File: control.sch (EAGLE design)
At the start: 123 parts, among them IC3 ATTINY85-20S, U1 L293DD013TR

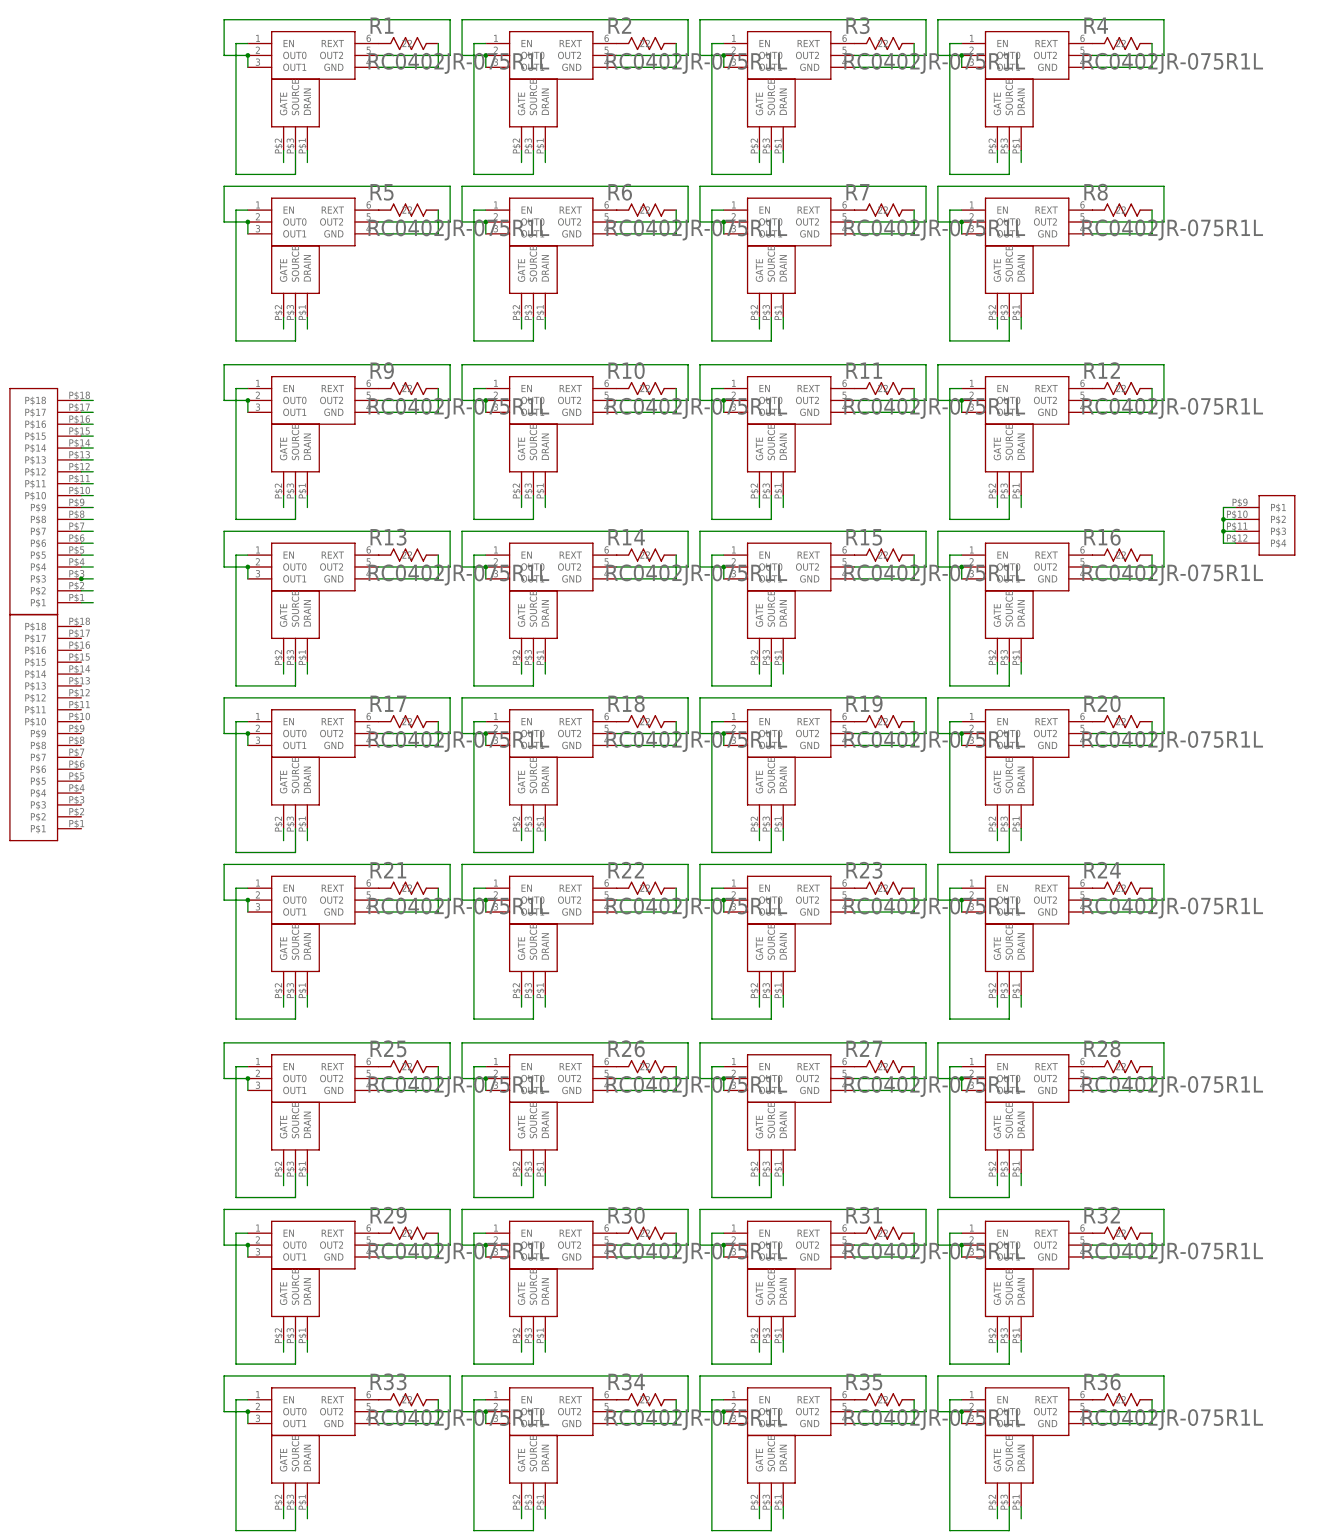
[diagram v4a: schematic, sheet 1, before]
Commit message: removes excess led controllers
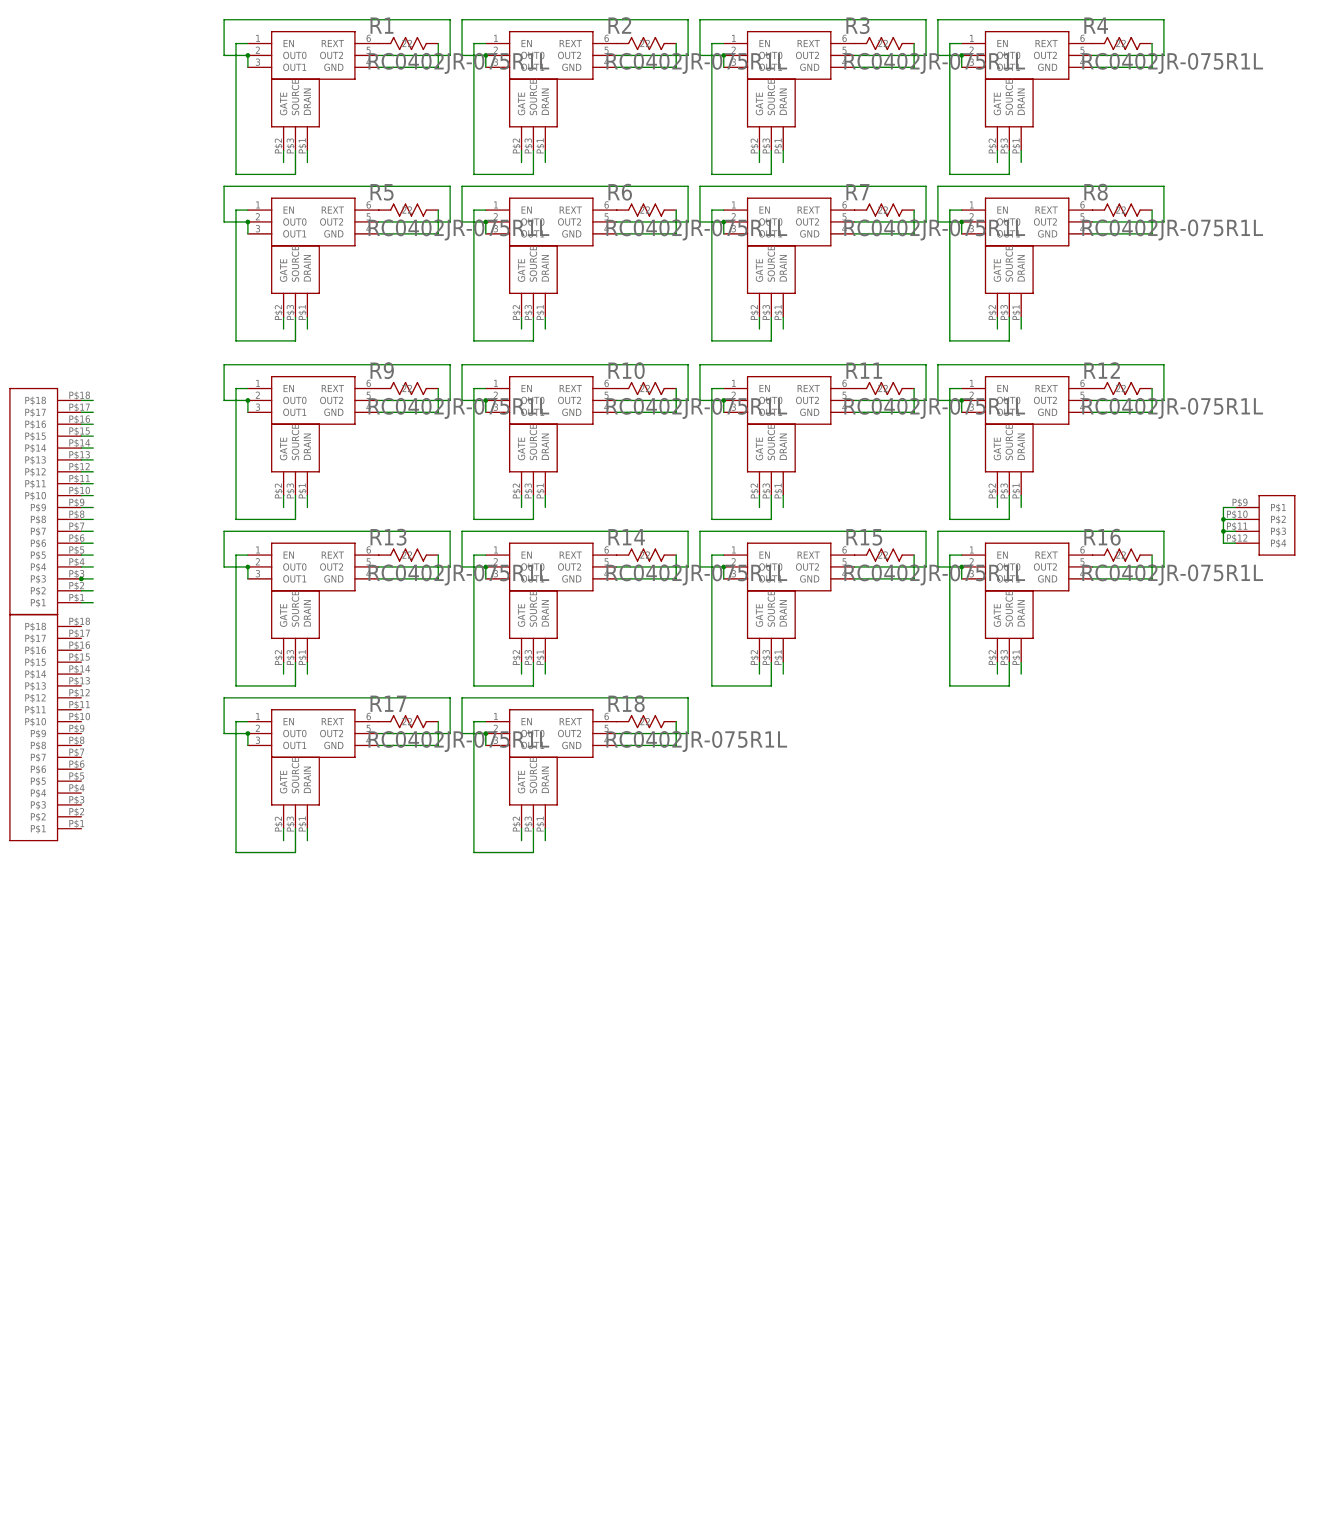
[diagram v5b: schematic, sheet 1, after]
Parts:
- removed C1: UVR0J102MPD1TA, Smile_Shade:UVR0J102MPD1TA
- removed C2: UWX1C101MCL1GB, Smile_Shade:UWX1C101MCL1GB
- removed R19, R20, R21, R22, R23, R24, R25, R26, R27, R28, R29, R30, R31, R32, R33, R34, R35, R36: RC0402JR-075R1L, Smile_Shade:RC0402JR-075R1L
- removed U$36: SRN8040-101M, Smile_Shade:SRN8040-101M
- removed U$41, U$46, U$48, U$50, U$52, U$54, U$56, U$58, U$60, U$62, U$64, U$66, U$68, U$70, U$72, U$74, U$76, U$78: 2N7002P, Smile_Shade:2N7002P
- removed U$43: LM2576HVSX-5.0/NOPB, Smile_Shade:LM2576HVSX-5.0/NOPB
- removed U$45, U$47, U$49, U$51, U$53, U$55, U$57, U$59, U$61, U$63, U$65, U$67, U$69, U$71, U$73, U$75, U$77, U$79: BCR420UW6-7, Smile_Shade:BCR420UW6-7
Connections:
- removed net 48V: C2.11
- removed net GND18: R19.11, U$41.DRAIN, U$45.GND
- removed net GND19: R20.11, U$46.DRAIN, U$47.GND
- removed net GND20: R21.11, U$48.DRAIN, U$49.GND
- removed net GND21: R22.11, U$50.DRAIN, U$51.GND
- removed net GND22: R23.11, U$52.DRAIN, U$53.GND
- removed net GND23: R24.11, U$54.DRAIN, U$55.GND
- removed net GND24: R25.11, U$56.DRAIN, U$57.GND
- removed net GND25: R26.11, U$58.DRAIN, U$59.GND
- removed net GND26: R27.11, U$60.DRAIN, U$61.GND
- removed net GND27: R28.11, U$62.DRAIN, U$63.GND
- removed net GND28: R29.11, U$64.DRAIN, U$65.GND
- removed net GND29: R30.11, U$66.DRAIN, U$67.GND
- removed net GND30: R31.11, U$68.DRAIN, U$69.GND
- removed net GND31: R32.11, U$70.DRAIN, U$71.GND
- removed net GND32: R33.11, U$72.DRAIN, U$73.GND
- removed net GND33: R34.11, U$74.DRAIN, U$75.GND
- removed net GND34: R35.11, U$76.DRAIN, U$77.GND
- removed net GND35: R36.11, U$78.DRAIN, U$79.GND
- removed net LEDSTR_33: U$45.OUT0, U$45.OUT1, U$45.OUT2
- removed net LEDSTR_34: U$47.OUT0, U$47.OUT1, U$47.OUT2
- removed net LEDSTR_35: U$49.OUT0, U$49.OUT1, U$49.OUT2
- removed net LEDSTR_36: U$51.OUT0, U$51.OUT1, U$51.OUT2
- removed net LEDSTR_37: U$53.OUT0, U$53.OUT1, U$53.OUT2
- removed net LEDSTR_38: U$55.OUT0, U$55.OUT1, U$55.OUT2
- removed net LEDSTR_39: U$57.OUT0, U$57.OUT1, U$57.OUT2
- removed net LEDSTR_40: U$59.OUT0, U$59.OUT1, U$59.OUT2
- removed net LEDSTR_41: U$61.OUT0, U$61.OUT1, U$61.OUT2
- removed net LEDSTR_42: U$63.OUT0, U$63.OUT1, U$63.OUT2
- removed net LEDSTR_43: U$65.OUT0, U$65.OUT1, U$65.OUT2
- removed net LEDSTR_44: U$67.OUT0, U$67.OUT1, U$67.OUT2
- removed net LEDSTR_45: U$69.OUT0, U$69.OUT1, U$69.OUT2
- removed net LEDSTR_46: U$71.OUT0, U$71.OUT1, U$71.OUT2
- removed net LEDSTR_47: U$73.OUT0, U$73.OUT1, U$73.OUT2
- removed net LEDSTR_48: U$75.OUT0, U$75.OUT1, U$75.OUT2
- removed net LEDSTR_49: U$77.OUT0, U$77.OUT1, U$77.OUT2
- removed net LEDSTR_50: U$79.OUT0, U$79.OUT1, U$79.OUT2
- removed net N$33: U$36.1, U$43.OUT
- removed net N$34: C2.22, U$43.VIN
- removed net N$42: U$41.SOURCE, U$45.EN
- removed net N$43: R19.22, U$45.REXT
- removed net N$44: U$46.SOURCE, U$47.EN
- removed net N$45: R20.22, U$47.REXT
- removed net N$46: U$48.SOURCE, U$49.EN
- removed net N$47: R21.22, U$49.REXT
- removed net N$48: U$50.SOURCE, U$51.EN
- removed net N$49: R22.22, U$51.REXT
- removed net N$50: U$52.SOURCE, U$53.EN
- removed net N$51: R23.22, U$53.REXT
- removed net N$52: U$54.SOURCE, U$55.EN
- removed net N$53: R24.22, U$55.REXT
- removed net N$54: U$56.SOURCE, U$57.EN
- removed net N$55: R25.22, U$57.REXT
- removed net N$56: U$58.SOURCE, U$59.EN
- removed net N$57: R26.22, U$59.REXT
- removed net N$58: U$60.SOURCE, U$61.EN
- removed net N$59: R27.22, U$61.REXT
- removed net N$60: U$62.SOURCE, U$63.EN
- removed net N$61: R28.22, U$63.REXT
- removed net N$62: U$64.SOURCE, U$65.EN
- removed net N$63: R29.22, U$65.REXT
- removed net N$64: U$66.SOURCE, U$67.EN
- removed net N$65: R30.22, U$67.REXT
- removed net N$66: U$68.SOURCE, U$69.EN
- removed net N$67: R31.22, U$69.REXT
- removed net N$68: U$70.SOURCE, U$71.EN
- removed net N$69: R32.22, U$71.REXT
- removed net N$70: U$72.SOURCE, U$73.EN
- removed net N$71: R33.22, U$73.REXT
- removed net N$72: U$74.SOURCE, U$75.EN
- removed net N$73: R34.22, U$75.REXT
- removed net N$74: U$76.SOURCE, U$77.EN
- removed net N$75: R35.22, U$77.REXT
- removed net N$76: U$78.SOURCE, U$79.EN
- removed net N$77: R36.22, U$79.REXT
- removed net ZN33: U$41.GATE
- removed net ZN34: U$46.GATE
- removed net ZN35: U$48.GATE
- removed net ZN36: U$50.GATE
- removed net ZN37: U$52.GATE
- removed net ZN38: U$54.GATE
- removed net ZN39: U$56.GATE
- removed net ZN40: U$58.GATE
- removed net ZN41: U$60.GATE
- removed net ZN42: U$62.GATE
- removed net ZN43: U$64.GATE
- removed net ZN44: U$66.GATE
- removed net ZN45: U$68.GATE
- removed net ZN46: U$70.GATE
- removed net ZN47: U$72.GATE
- removed net ZN48: U$74.GATE
- removed net ZN49: U$76.GATE
- removed net ZN50: U$78.GATE
- net 5V: no longer C1.22, U$36.2, U$43.FB
- net GND: no longer C1.11, U$43.GND, U$43.TAB, U$43.~ON~/OFF
